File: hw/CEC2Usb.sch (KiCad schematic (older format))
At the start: 33 parts, among them J1 USB_B_Mini, J2 HDMI_A, J3 HDMI_A, J4 ICSP, Q1 BC817, U1 TLV70233_SOT23-5, U2 ATmega32U2-AU, Y1 16MHz

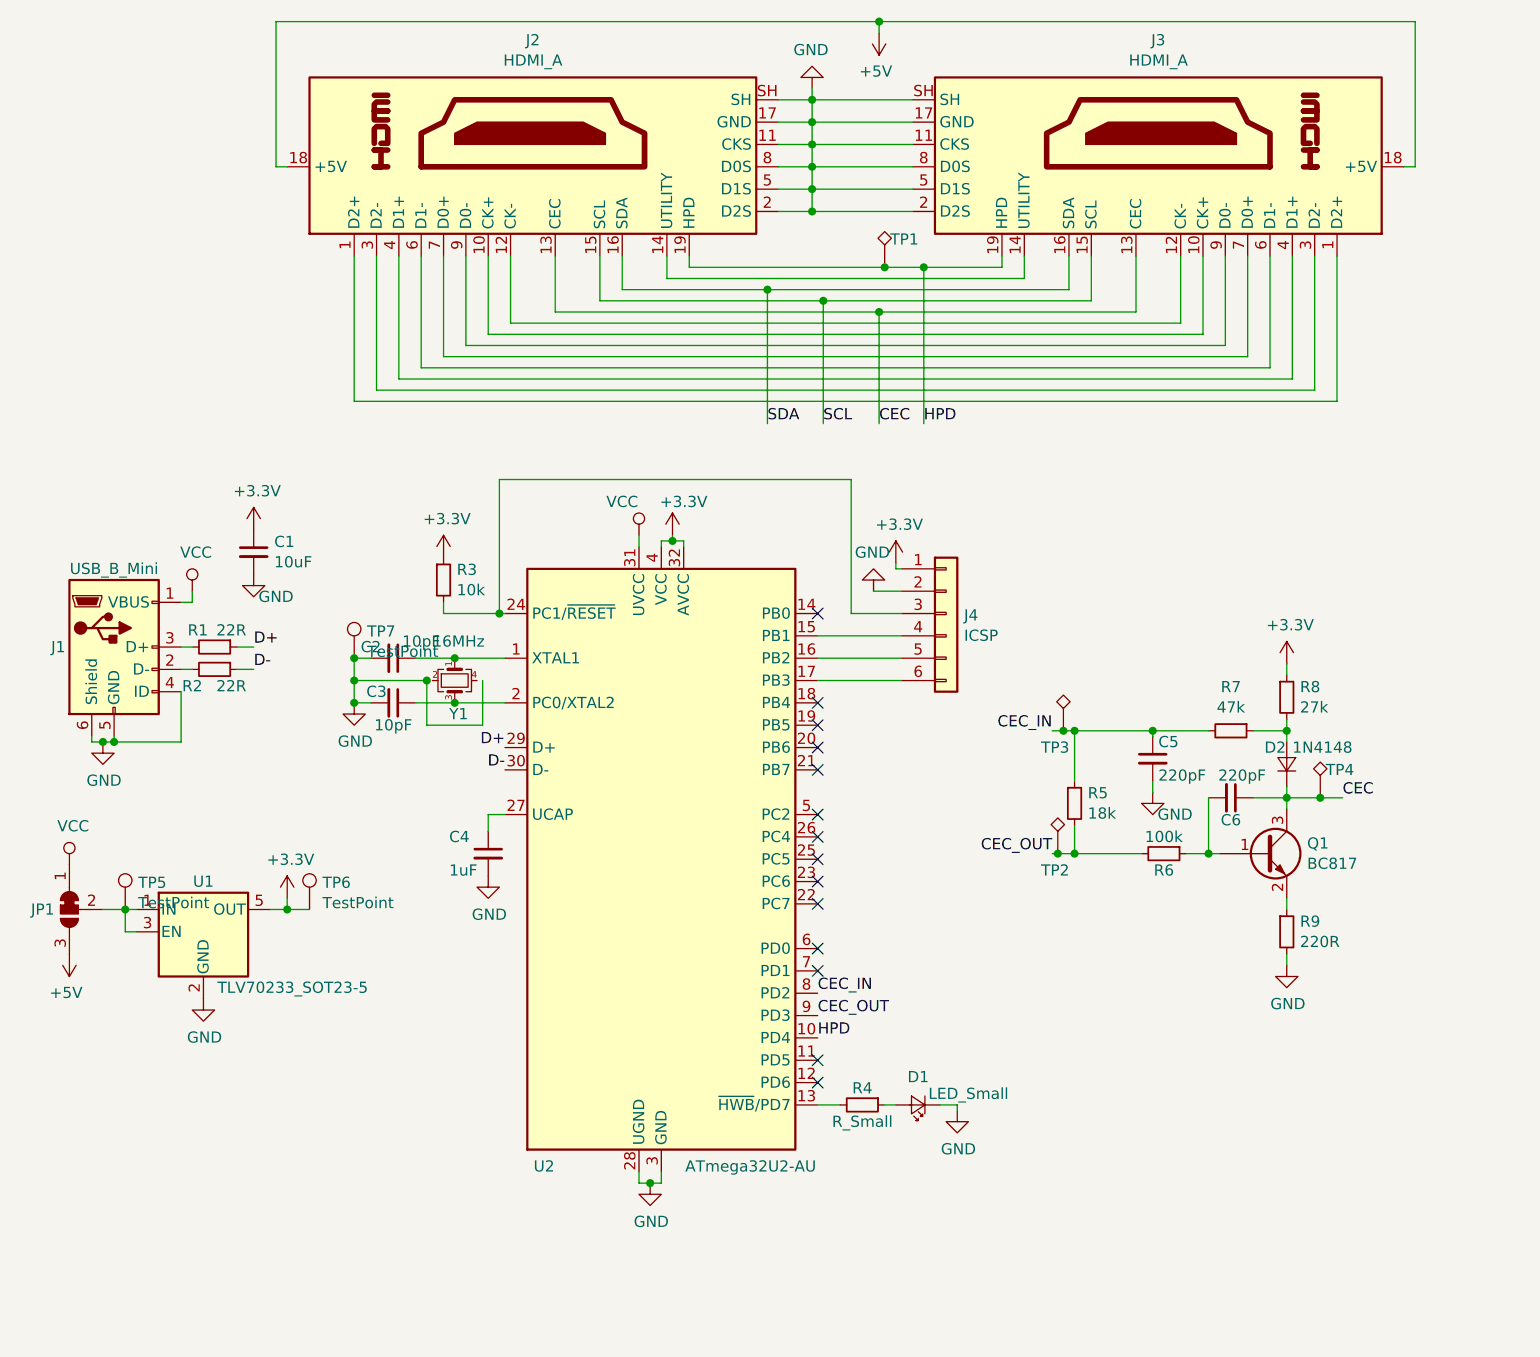
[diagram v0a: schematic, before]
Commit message: [Hw] v0.2, Fixed mistakes, moved stuff, add LEDs conn
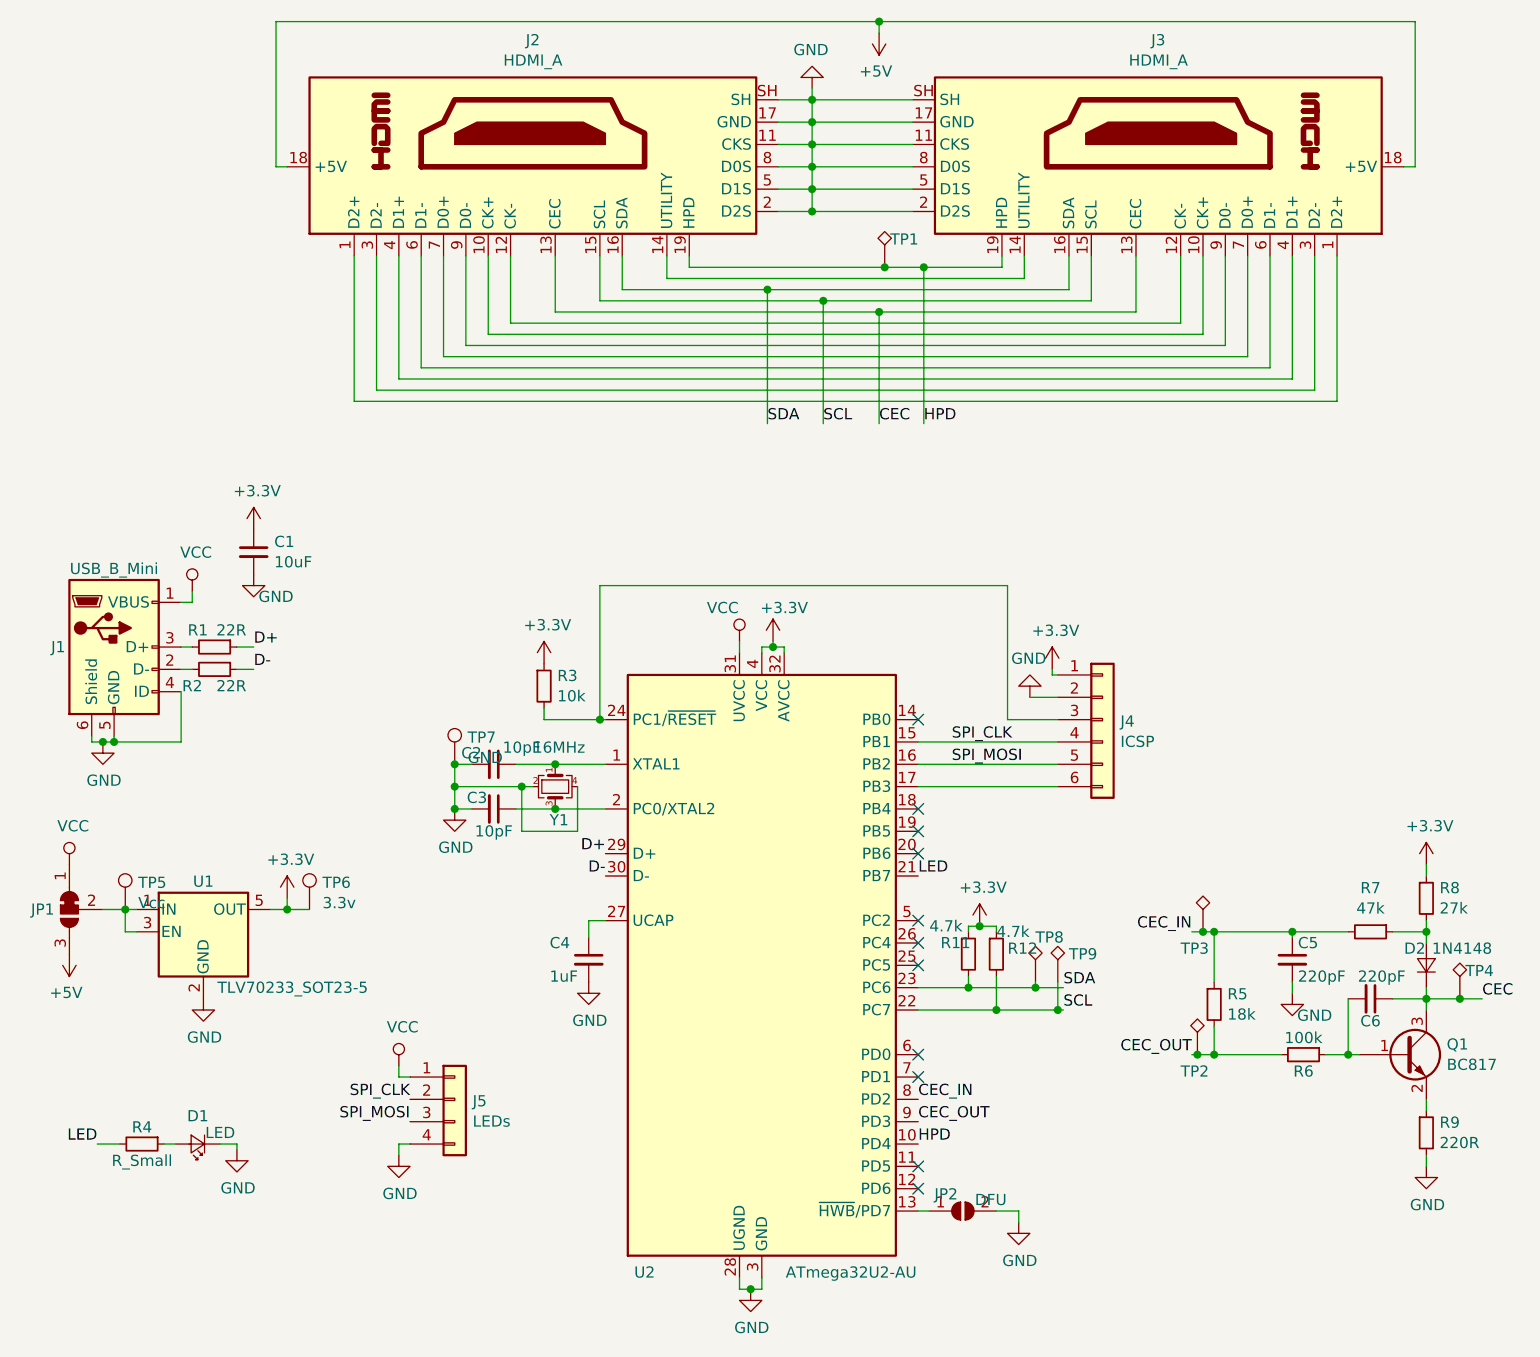
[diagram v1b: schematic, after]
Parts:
- added J5: LEDs, Connector_PinHeader_2.54mm:PinHeader_1x04_P2.54mm_Vertical, symbol Connector_Generic:Conn_01x04
- added JP2: DFU, Jumper:SolderJumper-2_P1.3mm_Open_RoundedPad1.0x1.5mm, symbol Jumper:SolderJumper_2_Open
- added R11, R12: 4.7k, Resistor_SMD:R_0603_1608Metric_Pad1.05x0.95mm_HandSolder, symbol Device:R_Small
- added TP8: SDA, TestPoint:TestPoint_Pad_1.5x1.5mm, symbol Connector:TestPoint_Alt
- added TP9: SCL, TestPoint:TestPoint_Pad_1.5x1.5mm, symbol Connector:TestPoint_Alt
- D1: value LED_Small -> LED
- TP1: value TestPoint_Alt -> HPD
- TP2: value TestPoint_Alt -> CEC_OUT
- TP3: value TestPoint_Alt -> CEC_IN
- TP4: value TestPoint_Alt -> CEC
- TP5: value TestPoint -> Vcc
- TP6: value TestPoint -> 3.3v
- TP7: value TestPoint -> GND
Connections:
- net +3V3: now also R11.1, R12.1
- net GND: now also Y1.2, Y1.4, J5.4 (Pin_4), JP2.2 (B)
- net SCL: now also U2.22 (PC7), R12.2, TP9.1
- net SDA: now also U2.23 (PC6), R11.2, TP8.1
- net VCC: now also J5.1 (Pin_1)
- net at U2.13 (~HWB~/PD7): now also JP2.1 (A); no longer R4.2
- net SPI_CLK: now reaches J4.4 (Pin_4), U2.15 (PB1)
- net SPI_CLK: now also J5.2 (Pin_2)
- net SPI_MOSI: now reaches J4.5 (Pin_5), U2.16 (PB2)
- net SPI_MOSI: now also J5.3 (Pin_3)
- net LED: now reaches U2.21 (PB7)
- net LED: now also R4.2
- no-connect marks 14 -> 11
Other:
- moved on the sheet: C2, C3, C4, C5, C6, D1, D2, J4, Q1, R3, R4, R5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
